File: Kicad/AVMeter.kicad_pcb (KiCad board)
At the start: 2 copper layers, 80 x 54 mm, 62 parts, among them J1 Conn_01x16, J6 Conn_02x03_Odd_Even, J7 Conn_01x02, J8 Conn_01x02, U1 LT6105, U2 LT6105, U3 LT6105, U4 LM321, U5 MCP3208, U6 ATmega328-PU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

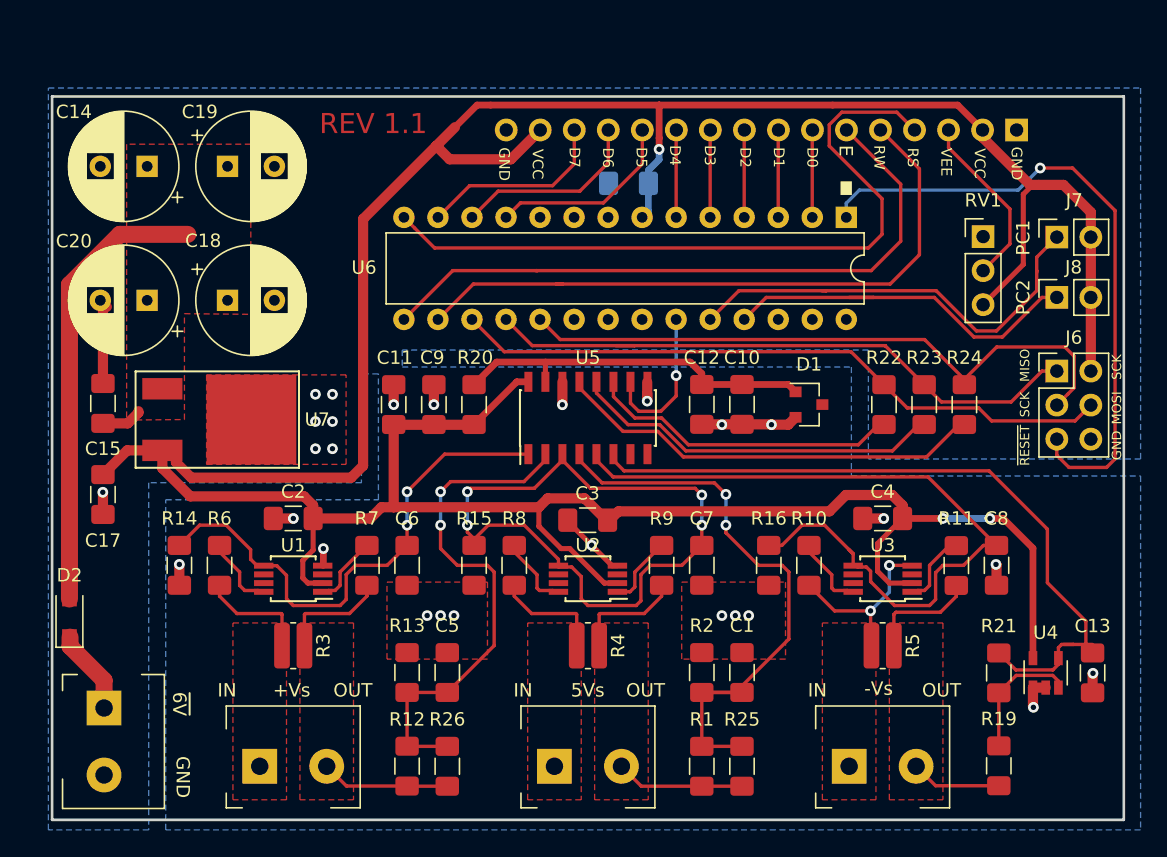
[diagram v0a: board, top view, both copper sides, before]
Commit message: fix for LM6105
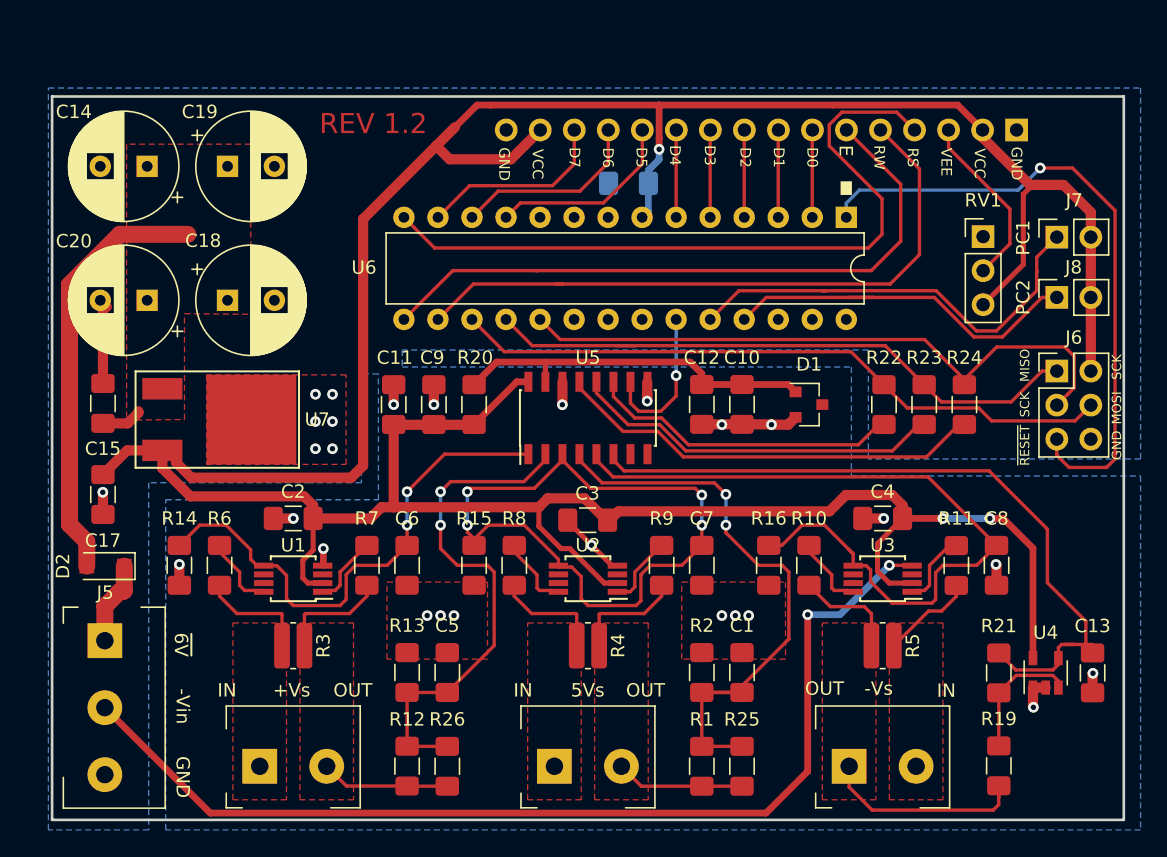
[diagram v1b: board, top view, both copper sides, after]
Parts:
- removed ~6V: Screw_Terminal_01x02, AVMeter:KF301_2Pin_5Pitch
- added J5: Screw_Terminal_01x03, AVMeter:KF301_3Pin_5Pitch, F.Cu at (191.5, 138.7)
- moved D2 4.70 mm to (191.6, 128.1), turned to 180 degrees
- renumbered +Vs to J2, 5Vs to J3, -Vs to J4
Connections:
- D2 pad 1: +6V -> +6Vin
- J4 pad 1: -Vs -> -Vs_Out
- J4 pad 2: -Vs_Out -> -Vs
- R10 pad 1: -Vs -> -Vs_Out
- R11 pad 1: -Vs_Out -> -Vs
- R5 pad 1: -Vs -> -Vs_Out
- R5 pad 2: -Vs_Out -> -Vs
- U3 pad 4: -Vs -> -Vin
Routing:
- net -Vin: track 0.00 -> 78.0 mm, vias 0 -> 2
- net -Vs_Out: track 15.1 -> 23.0 mm
- net -Vs: track 13.7 -> 7.00 mm, vias 2 -> 0
- net +6V: track 6.41 -> 0.00 mm
- net +6Vin: track 0.00 -> 6.33 mm
- net Net-(C14-Pad1): track 36.9 -> 35.0 mm
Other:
- board text added: "-Vin"
- board text added: "REV 1.2"
- board text removed: "REV 1.1"

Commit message: added mount holes and other
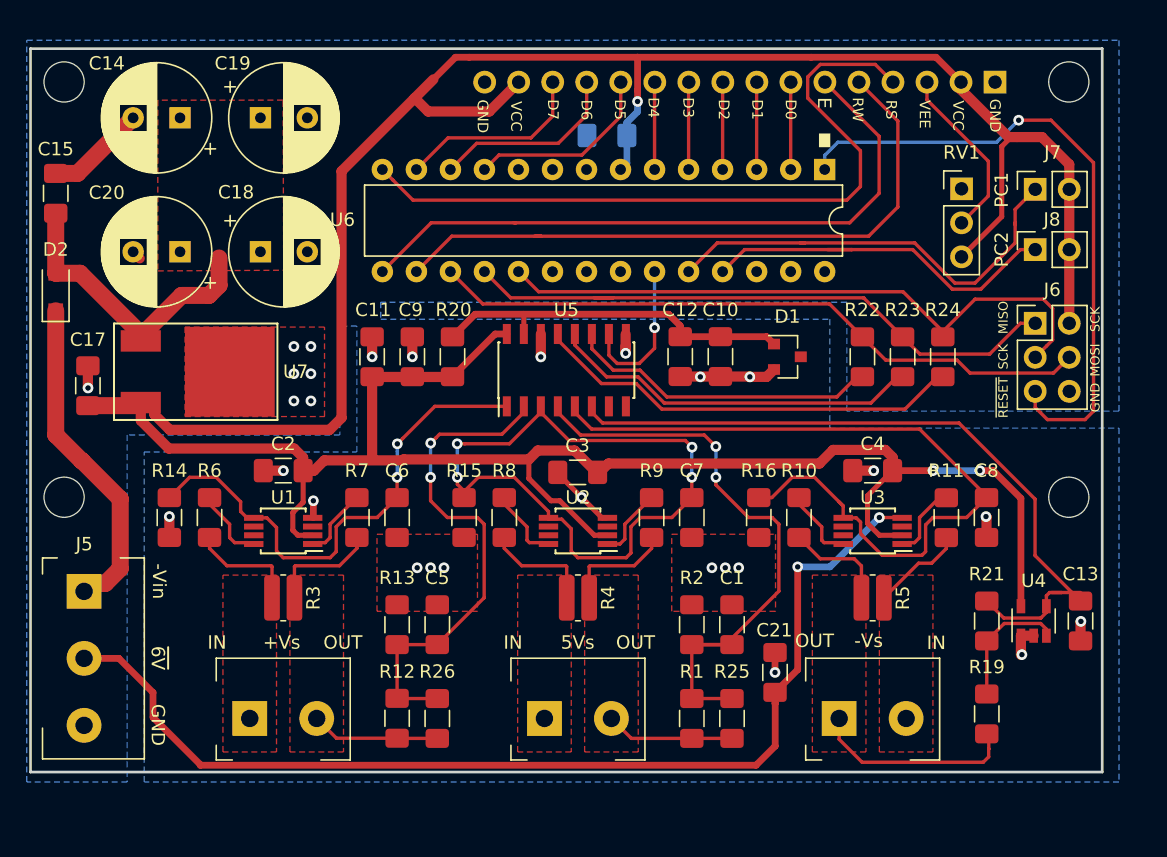
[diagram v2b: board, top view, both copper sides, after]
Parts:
- added C21: 220nf, Capacitor_SMD:C_1206_3216Metric_Pad1.42x1.75mm_HandSolder, F.Cu at (241.6, 136.1)
- added REF**: MountingHole_3mm, MountingHole:MountingHole_3mm, F.Cu at (263.5, 92.0)
- added REF**: MountingHole_3mm, MountingHole:MountingHole_3mm, F.Cu at (188.5, 123.0)
- added REF**: MountingHole_3mm, MountingHole:MountingHole_3mm, F.Cu at (188.5, 92.0)
- added REF**: MountingHole_3mm, MountingHole:MountingHole_3mm, F.Cu at (263.5, 123.0)
- moved D2 20.8 mm to (187.9, 107.7), turned to 90 degrees
- moved C15 16.1 mm to (187.9, 100.3)
- moved C17 8.20 mm to (190.3, 114.7), turned to 90 degrees
- moved C14 4.37 mm to (197.2, 94.7)
- moved C18 4.37 mm to (203.2, 104.7)
- moved C19 4.37 mm to (203.2, 94.7)
- moved C20 4.37 mm to (197.2, 104.7)
- moved J5 3.99 mm to (190.0, 135.0)
- moved R19 3.98 mm to (257.4, 139.2)
- moved C13 3.98 mm to (264.4, 132.2)
- moved R21 3.98 mm to (257.4, 132.2)
- moved U4 3.98 mm to (260.9, 132.2)
- moved U6 3.92 mm to (245.3, 98.5)
- moved RV1 3.92 mm to (255.5, 100.0)
- moved C16 3.92 mm to (229.0, 96.0)
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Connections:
- U5 pad 7: (no net) -> Net-(U5-Pad7)
- U5 pad 8: (no net) -> Net-(U5-Pad8)
- U6 pad 10: (no net) -> Net-(U6-Pad10)
- U6 pad 20: (no net) -> Net-(U6-Pad20)
- U6 pad 21: (no net) -> Net-(U6-Pad21)
- U6 pad 26: (no net) -> Net-(U6-Pad26)
- U6 pad 27: (no net) -> Net-(U6-Pad27)
- U6 pad 28: (no net) -> Net-(U6-Pad28)
- U6 pad 9: (no net) -> Net-(U6-Pad9)
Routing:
- net +6Vin: track 6.33 -> 24.7 mm
- net Net-(C14-Pad1): track 35.0 -> 23.1 mm
- net GND: track 41.4 -> 44.3 mm, vias 27 -> 28
- net -Vin: track 78.0 -> 80.0 mm
- net -I_ADC: track 57.4 -> 58.4 mm
- net +I_ADC: track 38.7 -> 37.9 mm
- net 5Vs_ADC: track 44.4 -> 45.3 mm
- net +Vs_ADC: track 38.9 -> 38.1 mm
- net VCC: track 264.9 -> 264.2 mm
- net -Vs_ADC: track 55.5 -> 55.0 mm
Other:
- board text removed: "REV 1.2"

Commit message: release V 1.2
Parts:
- moved R19 0.32 mm to (257.4, 139.5)
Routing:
- net Net-(C14-Pad1): track 23.1 -> 36.4 mm
- net -Vs_Out: track 23.0 -> 22.5 mm
